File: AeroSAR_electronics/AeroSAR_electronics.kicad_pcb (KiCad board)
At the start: 2 copper layers, 80 x 120 mm, 5 parts, among them J1 USB_B_Micro

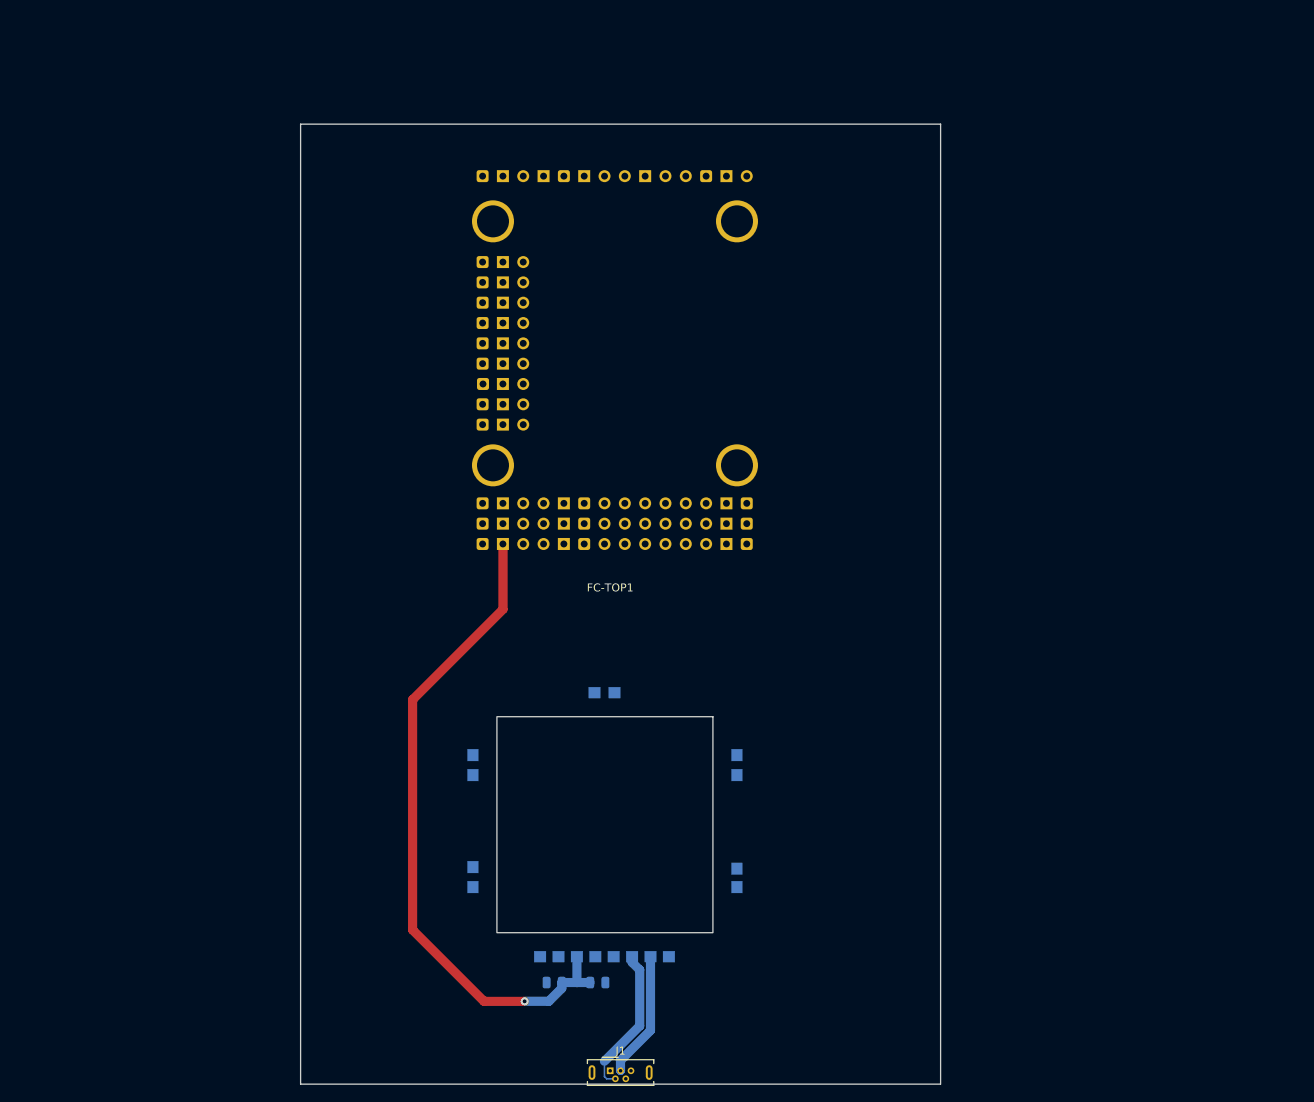
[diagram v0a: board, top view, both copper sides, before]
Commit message: Added terminals and reworked USB implementation
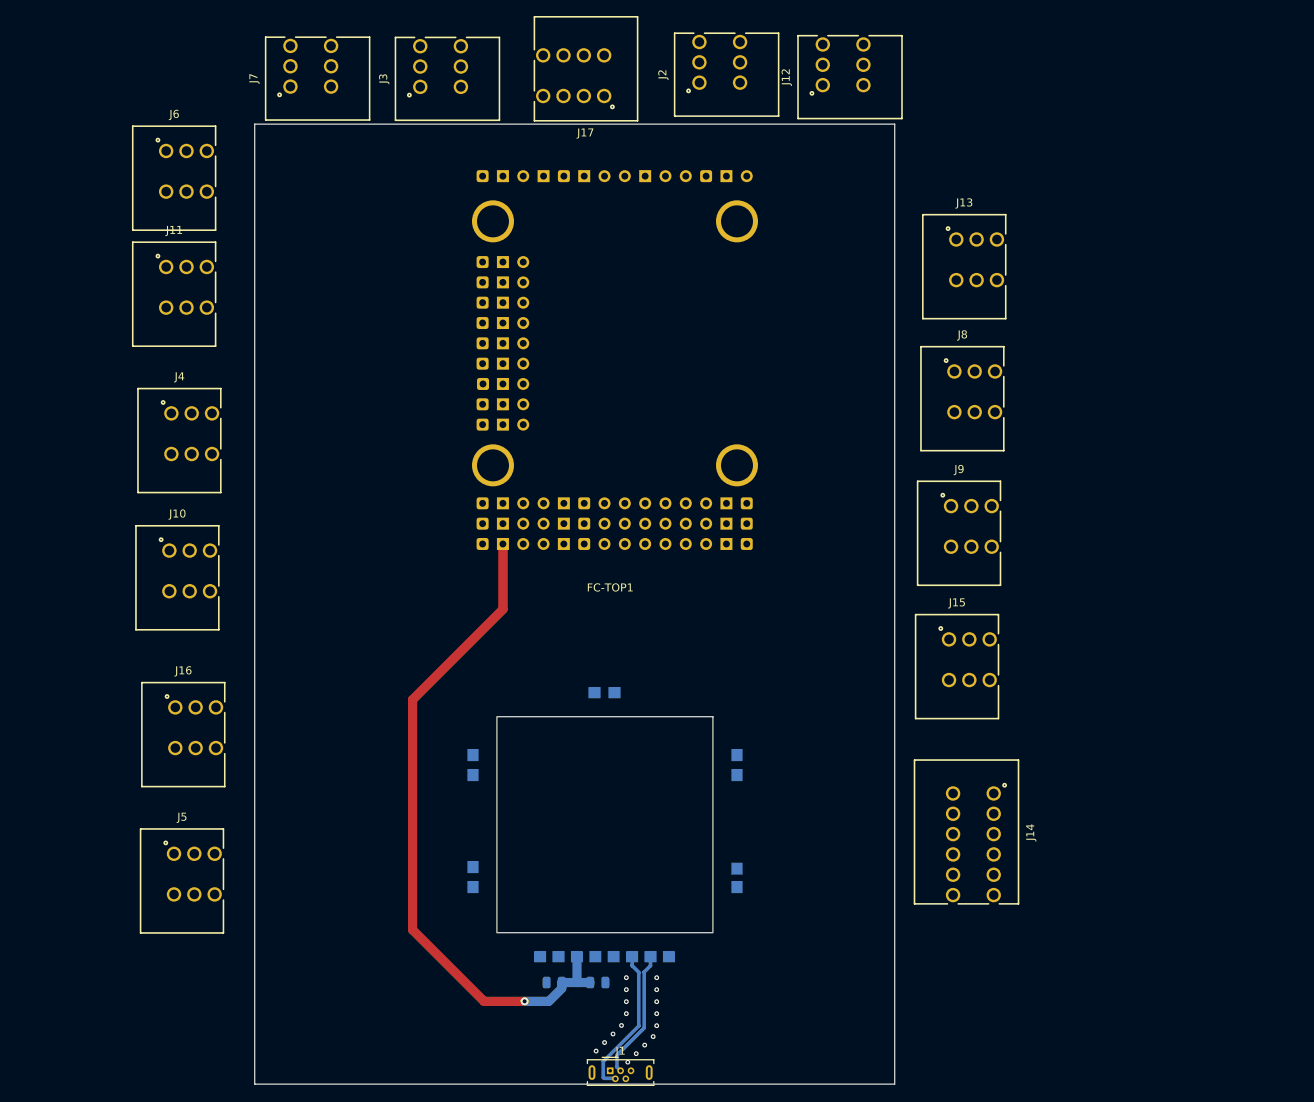
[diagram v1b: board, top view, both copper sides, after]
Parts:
- added J10: Servo, BL-M8812EU3:691403900003B, F.Cu at (86.5, 95.8)
- added J11: Servo, BL-M8812EU3:691403900003B, F.Cu at (86.1, 60.4)
- added J12: Servo, BL-M8812EU3:691403900003B, F.Cu at (168.2, 32.6)
- added J13: Servo, BL-M8812EU3:691403900003B, F.Cu at (184.9, 57.0)
- added J14: NAV Module, BL-M8812EU6:691403900006B, F.Cu at (184.5, 130.0)
- added J15: RPI, BL-M8812EU3:691403900003B, F.Cu at (184.0, 106.9)
- added J16: Receiver, BL-M8812EU3:691403900003B, F.Cu at (87.3, 115.4)
- added J17: PDB, BL-M8812EU4:691403900004B, F.Cu at (134.5, 33.9)
- added J2: ESC-1, BL-M8812EU3:691403900003B, F.Cu at (152.8, 32.3)
- added J3: ESC-2, BL-M8812EU3:691403900003B, F.Cu at (117.9, 32.8)
- added J4: Servo, BL-M8812EU3:691403900003B, F.Cu at (86.8, 78.7)
- added J5: Servo, BL-M8812EU3:691403900003B, F.Cu at (87.1, 133.7)
- added J6: Servo, BL-M8812EU3:691403900003B, F.Cu at (86.1, 45.9)
- added J7: Servo, BL-M8812EU3:691403900003B, F.Cu at (101.7, 32.8)
- added J8: Servo, BL-M8812EU3:691403900003B, F.Cu at (184.7, 73.5)
- added J9: Servo, BL-M8812EU3:691403900003B, F.Cu at (184.2, 90.3)
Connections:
- net Net-(J1-D+) renamed /D+
- net Net-(J1-D-) renamed /D-
- FC-TOP1 pad 10: GND-PDB -> Net-(FC-TOP1-GND-Pad10)
- FC-TOP1 pad 11: VCC-PDB -> Net-(FC-TOP1-Vx-Pad11)
- FC-TOP1 pad 2: unconnected-(FC-TOP1-5V-Pad2) -> Net-(FC-TOP1-5V-Pad2)
- FC-TOP1 pad 21: unconnected-(FC-TOP1-GND-Pad21) -> Net-(FC-TOP1-GND-Pad21)
- FC-TOP1 pad 22: unconnected-(FC-TOP1-GND-Pad22) -> Net-(FC-TOP1-GND-Pad22)
- FC-TOP1 pad 23: GND-Receiver -> Net-(FC-TOP1-GND-Pad23)
- FC-TOP1 pad 3: unconnected-(FC-TOP1-GND-Pad3) -> Net-(FC-TOP1-GND-Pad3)
- FC-TOP1 pad 30: unconnected-(FC-TOP1-Vx-Pad30) -> Net-(FC-TOP1-Vx-Pad30)
- FC-TOP1 pad 31: unconnected-(FC-TOP1-Vx-Pad31) -> Net-(FC-TOP1-Vx-Pad31)
- FC-TOP1 pad 32: VCC-Receiver -> Net-(FC-TOP1-Vx-Pad32)
- FC-TOP1 pad 39: unconnected-(FC-TOP1-S8-Pad39) -> Net-(FC-TOP1-S8)
- FC-TOP1 pad 40: unconnected-(FC-TOP1-S9-Pad40) -> Net-(FC-TOP1-S9)
- FC-TOP1 pad 41: unconnected-(FC-TOP1-S10-Pad41) -> Net-(FC-TOP1-S10)
- FC-TOP1 pad 42: unconnected-(FC-TOP1-GND-Pad42) -> Net-(FC-TOP1-GND-Pad42)
- FC-TOP1 pad 43: unconnected-(FC-TOP1-Vx-Pad43) -> Net-(FC-TOP1-Vx-Pad43)
- FC-TOP1 pad 44: unconnected-(FC-TOP1-S11-Pad44) -> Net-(FC-TOP1-S11)
- FC-TOP1 pad 55: unconnected-(FC-TOP1-GND-Pad55) -> RPI_GND
- FC-TOP1 pad 56: unconnected-(FC-TOP1-GND-Pad56) -> Net-(FC-TOP1-GND-Pad56)
- FC-TOP1 pad 57: unconnected-(FC-TOP1-Vx-Pad57) -> Net-(FC-TOP1-Vx-Pad57)
- FC-TOP1 pad 58: unconnected-(FC-TOP1-S12-Pad58) -> Net-(FC-TOP1-S12)
- FC-TOP1 pad 64: Net-(FC-TOP1-DA1-Pad64) -> /NAV_COMPASS_DA
- FC-TOP1 pad 65: Net-(FC-TOP1-CL1-Pad65) -> /NAV_COMPASS_CL
- FC-TOP1 pad 66: Net-(FC-TOP1-Tx2) -> /NAV_GPS_TX
- FC-TOP1 pad 67: Net-(FC-TOP1-Rx2) -> /NAV_GPS_RX
- FC-TOP1 pad 79: Net-(FC-TOP1-Rx4) -> /Receiver
- FC-TOP1 pad 8: unconnected-(FC-TOP1-Curr-Pad8) -> Net-(FC-TOP1-Curr)
- FC-TOP1 pad 82: VCC-GPS&Compass -> Net-(FC-TOP1-4V5-Pad82)
- FC-TOP1 pad 83: GND-GPS&Compass -> Net-(FC-TOP1-GND-Pad83)
- FC-TOP1 pad 9: unconnected-(FC-TOP1-Vbat-Pad9) -> Net-(FC-TOP1-Vbat)
- WiFi_module1 pad 5: unconnected-(WiFi_module1-RST-Pad5) -> Net-(WiFi_module1-RST)
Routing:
- net (no net): vias 0 -> 17

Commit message: Wired terminal, added mounting holes and copper zones with via stitching
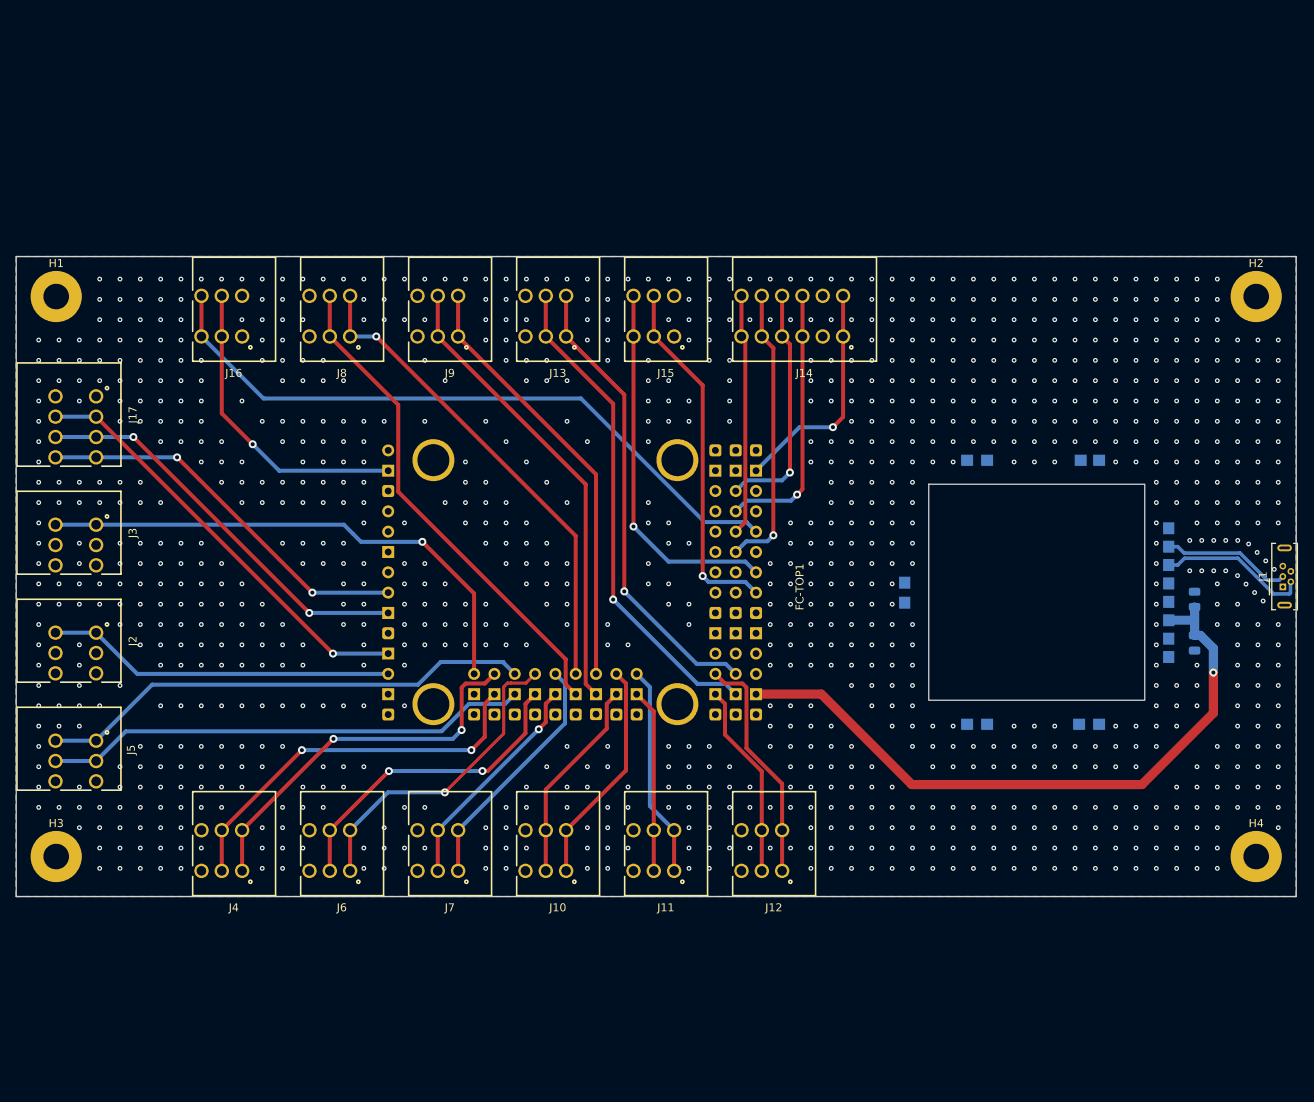
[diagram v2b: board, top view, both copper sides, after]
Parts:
- added H1: MountingHole_Pad, MountingHole:MountingHole_3.2mm_M3_Pad, F.Cu at (69.8, 61.5)
- added H2: MountingHole_Pad, MountingHole:MountingHole_3.2mm_M3_Pad, F.Cu at (219.8, 61.5)
- added H3: MountingHole_Pad, MountingHole:MountingHole_3.2mm_M3_Pad, F.Cu at (69.8, 131.6)
- added H4: MountingHole_Pad, MountingHole:MountingHole_3.2mm_M3_Pad, F.Cu at (219.8, 131.6)
- moved J2 109.2 mm to (72.3, 106.1), turned to -90 degrees
- moved J1 103.6 mm to (223.2, 97.8), turned to 90 degrees
- moved J7 99.3 mm to (117.5, 130.8), turned to 180 degrees
- moved J12 98.7 mm to (158.1, 130.8), turned to 180 degrees
- moved J11 91.5 mm to (144.6, 130.8), turned to 180 degrees
- moved C2 90.6 mm to (212.2, 104.8), turned to -90 degrees
- moved C1 88.7 mm to (212.2, 99.4), turned to 90 degrees
- moved J6 86.8 mm to (104.0, 130.8), turned to 180 degrees
- moved J8 81.2 mm to (104.0, 64.0), turned to 180 degrees
- moved J17 76.2 mm to (72.3, 77.8), turned to -90 degrees
- moved J3 75.2 mm to (72.3, 92.6), turned to -90 degrees
- moved J9 71.7 mm to (117.5, 64.0), turned to 180 degrees
- moved FC-TOP1 71.4 mm to (109.8, 115.2), turned to 90 degrees
- moved J14 69.8 mm to (161.9, 64.0), turned to 180 degrees
- moved J15 58.3 mm to (144.6, 64.0), turned to 180 degrees
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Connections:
- FC-TOP1 pad 10: Net-(FC-TOP1-GND-Pad10) -> GND
- FC-TOP1 pad 14: Net-(FC-TOP1-GND-Pad14) -> GND
- FC-TOP1 pad 15: Net-(FC-TOP1-GND-Pad15) -> GND
- FC-TOP1 pad 16: Net-(FC-TOP1-GND-Pad16) -> GND
- FC-TOP1 pad 17: Net-(FC-TOP1-GND-Pad17) -> GND
- FC-TOP1 pad 18: Net-(FC-TOP1-GND-Pad18) -> GND
- FC-TOP1 pad 19: Net-(FC-TOP1-GND-Pad19) -> GND
- FC-TOP1 pad 20: Net-(FC-TOP1-GND-Pad20) -> GND
- FC-TOP1 pad 21: Net-(FC-TOP1-GND-Pad21) -> GND
- FC-TOP1 pad 22: Net-(FC-TOP1-GND-Pad22) -> GND
- FC-TOP1 pad 23: Net-(FC-TOP1-GND-Pad23) -> GND
- FC-TOP1 pad 3: Net-(FC-TOP1-GND-Pad3) -> GND
- FC-TOP1 pad 42: Net-(FC-TOP1-GND-Pad42) -> GND
- FC-TOP1 pad 55: RPI_GND -> GND
- FC-TOP1 pad 56: Net-(FC-TOP1-GND-Pad56) -> GND
- FC-TOP1 pad 70: GND-WiFi -> GND
- J10 pad 3: Net-(FC-TOP1-GND-Pad22) -> GND
- J10 pad A3: Net-(FC-TOP1-GND-Pad22) -> GND
- J11 pad 3: Net-(FC-TOP1-GND-Pad23) -> GND
- J11 pad A3: Net-(FC-TOP1-GND-Pad23) -> GND
- J12 pad 3: Net-(FC-TOP1-GND-Pad42) -> GND
- J12 pad A3: Net-(FC-TOP1-GND-Pad42) -> GND
- J13 pad 3: Net-(FC-TOP1-GND-Pad56) -> GND
- J13 pad A3: Net-(FC-TOP1-GND-Pad56) -> GND
- J15 pad 1: RPI_GND -> GND
- J15 pad A1: RPI_GND -> GND
- J16 pad 1: Net-(FC-TOP1-GND-Pad3) -> GND
- J16 pad A1: Net-(FC-TOP1-GND-Pad3) -> GND
- J17 pad 1: Net-(FC-TOP1-GND-Pad10) -> GND
- J17 pad A1: Net-(FC-TOP1-GND-Pad10) -> GND
- J2 pad 3: Net-(FC-TOP1-GND-Pad14) -> GND
- J2 pad A3: Net-(FC-TOP1-GND-Pad14) -> GND
- J3 pad 3: Net-(FC-TOP1-GND-Pad15) -> GND
- J3 pad A3: Net-(FC-TOP1-GND-Pad15) -> GND
- J4 pad 3: Net-(FC-TOP1-GND-Pad16) -> GND
- J4 pad A3: Net-(FC-TOP1-GND-Pad16) -> GND
- J5 pad 3: Net-(FC-TOP1-GND-Pad17) -> GND
- J5 pad A3: Net-(FC-TOP1-GND-Pad17) -> GND
- J6 pad 3: Net-(FC-TOP1-GND-Pad18) -> GND
- J6 pad A3: Net-(FC-TOP1-GND-Pad18) -> GND
- J7 pad 3: Net-(FC-TOP1-GND-Pad19) -> GND
- J7 pad A3: Net-(FC-TOP1-GND-Pad19) -> GND
- J8 pad 3: Net-(FC-TOP1-GND-Pad20) -> GND
- J8 pad A3: Net-(FC-TOP1-GND-Pad20) -> GND
- J9 pad 3: Net-(FC-TOP1-GND-Pad21) -> GND
- J9 pad A3: Net-(FC-TOP1-GND-Pad21) -> GND
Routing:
- net /Receiver: track 0.00 -> 84.5 mm
- net Net-(FC-TOP1-S2): track 0.00 -> 65.9 mm, vias 0 -> 1
- net Net-(FC-TOP1-Vx-Pad29): track 0.00 -> 62.5 mm
- net Net-(FC-TOP1-S4): track 0.00 -> 62.1 mm
- net Net-(FC-TOP1-Vx-Pad57): track 0.00 -> 61.7 mm, vias 0 -> 1
- net Net-(FC-TOP1-Vx-Pad26): track 0.00 -> 60.9 mm
- net Net-(FC-TOP1-S7): track 0.00 -> 60.9 mm, vias 0 -> 1
- net Net-(FC-TOP1-Vx-Pad30): track 0.00 -> 58.3 mm
- net Net-(FC-TOP1-S12): track 0.00 -> 58.2 mm, vias 0 -> 1
- net Net-(FC-TOP1-S8): track 0.00 -> 54.4 mm
- net Net-(FC-TOP1-Vx-Pad11): track 0.00 -> 53.9 mm, vias 0 -> 1
- net Net-(FC-TOP1-Vbat): track 0.00 -> 50.7 mm, vias 0 -> 2
- net Net-(FC-TOP1-Vx-Pad25): track 0.00 -> 48.6 mm, vias 0 -> 2
- net Net-(FC-TOP1-Curr): track 0.00 -> 48.6 mm, vias 0 -> 2
- net Net-(FC-TOP1-S3): track 0.00 -> 47.8 mm, vias 0 -> 2
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- added copper zone on B.Cu, net GND
- added copper zone on F.Cu, net GND
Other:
- board size 80 x 120 mm -> 160 x 80 mm
